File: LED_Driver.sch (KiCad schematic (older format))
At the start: 0 parts

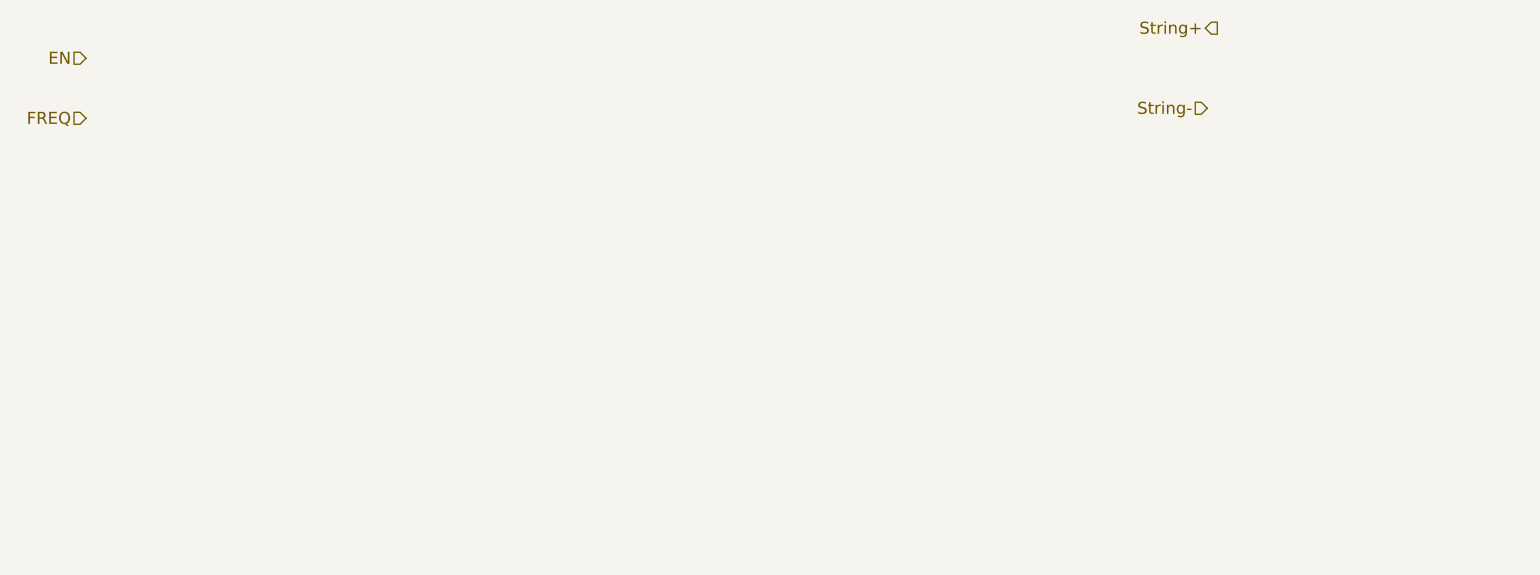
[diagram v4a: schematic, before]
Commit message: Added LED Driver Module Outline
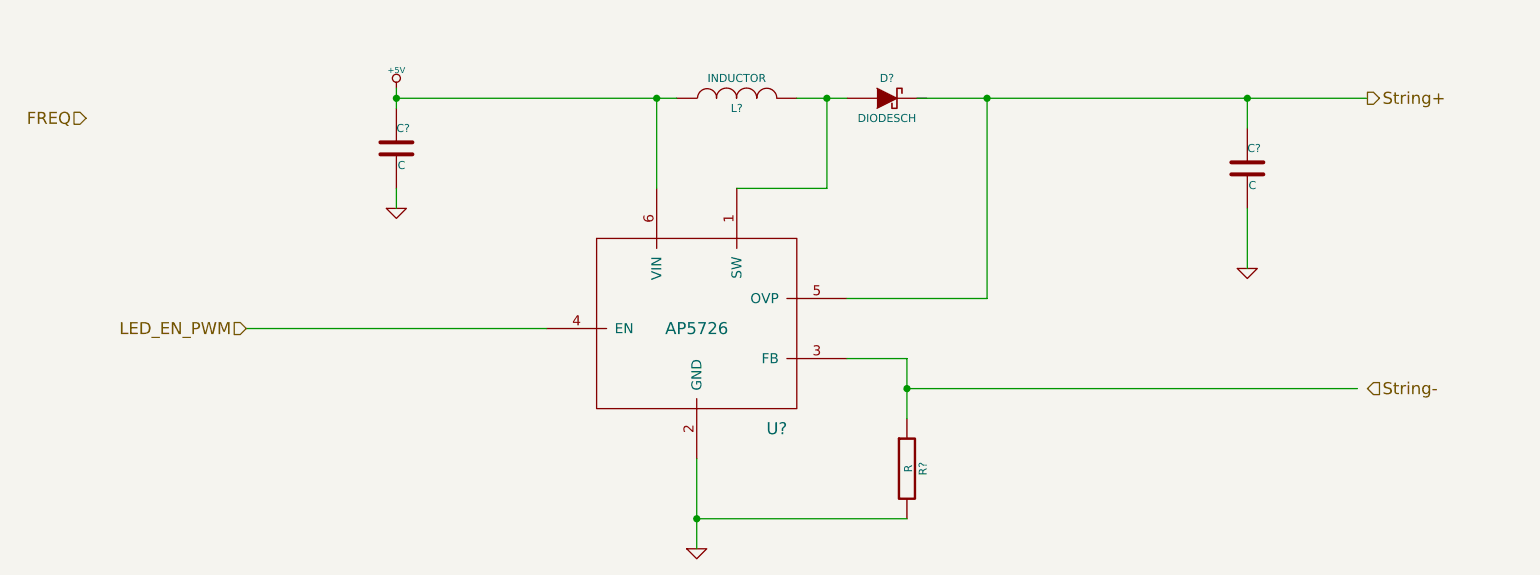
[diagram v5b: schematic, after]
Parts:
- added C? (x2): C, ~, symbol C
- added D?: DIODESCH, ~, symbol DIODESCH
- added L?: INDUCTOR, ~, symbol INDUCTOR
- added R?: R, ~, symbol R
- added U?: AP5726, symbol AP5726
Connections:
- net labels added: +5V, GND, LED_EN_PWM
- net labels removed: EN
- wire segments 0 -> 18
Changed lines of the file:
@@
 $Descr A4 11693 8268
 encoding utf-8
-Sheet 7 9
+Sheet 6 9
 Title ""
 Date "4 feb 2014"
@@
 Comment4 ""
 $EndDescr
-Text HLabel 2500 2350 0    60   Input ~ 0
-EN
+Text HLabel 3300 3700 0    60   Input ~ 0
+LED_EN_PWM
 Text HLabel 2500 2650 0    60   Input ~ 0
 FREQ
-Text HLabel 8150 2200 0    60   Output ~ 0
+Text HLabel 8900 2550 2    60   Output ~ 0
 String+
-Text HLabel 8100 2600 0    60   Input ~ 0
+Text HLabel 8900 4000 2    60   Input ~ 0
 String-
+$Comp
+L AP5726 U?
+U 1 1 52F0C98F
+P 5550 3700
+F 0 "U?" H 5950 3200 60  0000 C CNN
+F 1 "AP5726" H 5550 3700 60  0000 C CNN
+F 2 "" H 5550 3700 60  0000 C CNN
+F 3 "" H 5550 3700 60  0000 C CNN
+	1    5550 3700
+	1    0    0    -1
+$EndComp
+Wire Wire Line
+	3300 3700 4800 3700
+$Comp
+L +5V #PWR?
+U 1 1 52F0C9A4
+P 4050 2500
+F 0 "#PWR?" H 4050 2590 20  0001 C CNN
+F 1 "+5V" H 4050 2590 30  0000 C CNN
+F 2 "" H 4050 2500 60  0000 C CNN
+F 3 "" H 4050 2500 60  0000 C CNN
+	1    4050 2500
+	1    0    0    -1
+$EndComp
+$Comp
+L GND #PWR?
+U 1 1 52F0C9B3
+P 4050 3100
+F 0 "#PWR?" H 4050 3100 30  0001 C CNN
+F 1 "GND" H 4050 3030 30  0001 C CNN
+F 2 "" H 4050 3100 60  0000 C CNN
+F 3 "" H 4050 3100 60  0000 C CNN
+	1    4050 3100
+	1    0    0    -1
+$EndComp
+$Comp
+L GND #PWR?
+U 1 1 52F0C9C0
+P 5550 4800
+F 0 "#PWR?" H 5550 4800 30  0001 C CNN
+F 1 "GND" H 5550 4730 30  0001 C CNN
+F 2 "" H 5550 4800 60  0000 C CNN
+F 3 "" H 5550 4800 60  0000 C CNN
+	1    5550 4800
+	1    0    0    -1
+$EndComp
+$Comp
+L C C?
+U 1 1 52F0C9C8
+P 4050 2800
+F 0 "C?" H 4050 2900 40  0000 L CNN
+F 1 "C" H 4056 2715 40  0000 L CNN
+F 2 "~" H 4088 2650 30  0000 C CNN
+F 3 "~" H 4050 2800 60  0000 C CNN
+	1    4050 2800
+	1    0    0    -1
+$EndComp
+Wire Wire Line
+	4050 2500 4050 2600
+Wire Wire Line
+	4050 3000 4050 3100
+Wire Wire Line
+	4050 2550 5450 2550
+Wire Wire Line
+	5350 2550 5350 3000
+Connection ~ 4050 2550
+$Comp
+L INDUCTOR L?
+U 1 1 52F0C9F4
+P 5750 2550
+F 0 "L?" V 5700 2550 40  0000 C CNN
+F 1 "INDUCTOR" V 5850 2550 40  0000 C CNN
+F 2 "~" H 5750 2550 60  0000 C CNN
+F 3 "~" H 5750 2550 60  0000 C CNN
+	1    5750 2550
+	0    -1   -1   0
+$EndComp
+Connection ~ 5350 2550
+Wire Wire Line
+	5750 3000 6200 3000
+Wire Wire Line
+	6200 3000 6200 2550
+Wire Wire Line
+	6050 2550 6300 2550
+$Comp
+L DIODESCH D?
+U 1 1 52F0CA1B
+P 6500 2550
+F 0 "D?" H 6500 2650 40  0000 C CNN
+F 1 "DIODESCH" H 6500 2450 40  0000 C CNN
+F 2 "~" H 6500 2550 60  0000 C CNN
+F 3 "~" H 6500 2550 60  0000 C CNN
+	1    6500 2550
+	1    0    0    -1
+$EndComp
+Connection ~ 6200 2550
+Wire Wire Line
+	6650 2550 8900 2550
+$Comp
+L C C?
+U 1 1 52F0CA49
+P 8300 2900
+F 0 "C?" H 8300 3000 40  0000 L CNN
+F 1 "C" H 8306 2815 40  0000 L CNN
+F 2 "~" H 8338 2750 30  0000 C CNN
+F 3 "~" H 8300 2900 60  0000 C CNN
+	1    8300 2900
+	1    0    0    -1
+$EndComp
+Wire Wire Line
+	8300 2700 8300 2550
+Connection ~ 8300 2550
+Wire Wire Line
+	8300 3100 8300 3400
+$Comp
+L GND #PWR?
+U 1 1 52F0CA75
+P 8300 3400
+F 0 "#PWR?" H 8300 3400 30  0001 C CNN
+F 1 "GND" H 8300 3330 30  0001 C CNN
+F 2 "" H 8300 3400 60  0000 C CNN
+F 3 "" H 8300 3400 60  0000 C CNN
+	1    8300 3400
+	1    0    0    -1
+$EndComp
+Wire Wire Line
+	5550 4350 5550 4800
+$Comp
+L R R?
+U 1 1 52F0CAAA
+P 6600 4400
+F 0 "R?" V 6680 4400 40  0000 C CNN
+F 1 "R" V 6607 4401 40  0000 C CNN
+F 2 "~" V 6530 4400 30  0000 C CNN
+F 3 "~" H 6600 4400 30  0000 C CNN
+	1    6600 4400
+	1    0    0    -1
+$EndComp
+Wire Wire Line
+	6300 3850 6600 3850
+Wire Wire Line
+	6600 3850 6600 4150
+Wire Wire Line
+	6600 4650 5550 4650
+Connection ~ 5550 4650
+Wire Wire Line
+	8850 4000 6600 4000
+Connection ~ 6600 4000
+Wire Wire Line
+	7000 3550 7000 2550
+Connection ~ 7000 2550
+Wire Wire Line
+	7000 3550 6300 3550
 $EndSCHEMATC

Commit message: Hooked up top level schematic
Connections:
- net labels added: LED_STRING+, LED_STRING-
- net labels removed: String+, String-
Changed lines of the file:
@@
 FREQ
 Text HLabel 8900 2550 2    60   Output ~ 0
-String+
-Text HLabel 8900 4000 2    60   Input ~ 0
-String-
+LED_STRING+
+Text HLabel 8900 4000 2    60   Output ~ 0
+LED_STRING-
 $Comp
 L AP5726 U?
@@
 Connection ~ 5550 4650
 Wire Wire Line
-	8850 4000 6600 4000
+	6600 4000 8900 4000
 Connection ~ 6600 4000
 Wire Wire Line

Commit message: Fan Current module refactoring
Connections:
- net labels removed: FREQ
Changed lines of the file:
@@
 $Descr A4 11693 8268
 encoding utf-8
-Sheet 6 9
+Sheet 5 9
 Title ""
 Date "4 feb 2014"
@@
 Text HLabel 3300 3700 0    60   Input ~ 0
 LED_EN_PWM
-Text HLabel 2500 2650 0    60   Input ~ 0
-FREQ
 Text HLabel 8900 2550 2    60   Output ~ 0
 LED_STRING+

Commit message: Begin Associating relay Module
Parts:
- gave numbers to parts that had none: 6
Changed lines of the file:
@@
 LIBS:BenchBudEE
 LIBS:BenchBudEE-cache
-EELAYER 27 0
+EELAYER 24 0
 EELAYER END
 $Descr A4 11693 8268
@@
 LED_STRING-
 $Comp
-L AP5726 U?
+L AP5726 U5
 U 1 1 52F0C98F
 P 5550 3700
-F 0 "U?" H 5950 3200 60  0000 C CNN
+F 0 "U5" H 5950 3200 60  0000 C CNN
 F 1 "AP5726" H 5550 3700 60  0000 C CNN
 F 2 "" H 5550 3700 60  0000 C CNN
@@
 	3300 3700 4800 3700
 $Comp
-L +5V #PWR?
+L +5V #PWR26
 U 1 1 52F0C9A4
 P 4050 2500
-F 0 "#PWR?" H 4050 2590 20  0001 C CNN
+F 0 "#PWR26" H 4050 2590 20  0001 C CNN
 F 1 "+5V" H 4050 2590 30  0000 C CNN
 F 2 "" H 4050 2500 60  0000 C CNN
@@
 $EndComp
 $Comp
-L GND #PWR?
+L GND #PWR27
 U 1 1 52F0C9B3
 P 4050 3100
-F 0 "#PWR?" H 4050 3100 30  0001 C CNN
+F 0 "#PWR27" H 4050 3100 30  0001 C CNN
 F 1 "GND" H 4050 3030 30  0001 C CNN
 F 2 "" H 4050 3100 60  0000 C CNN
@@
 $EndComp
 $Comp
-L GND #PWR?
+L GND #PWR28
 U 1 1 52F0C9C0
 P 5550 4800
-F 0 "#PWR?" H 5550 4800 30  0001 C CNN
+F 0 "#PWR28" H 5550 4800 30  0001 C CNN
 F 1 "GND" H 5550 4730 30  0001 C CNN
 F 2 "" H 5550 4800 60  0000 C CNN
@@
 $EndComp
 $Comp
-L C C?
+L C C3
 U 1 1 52F0C9C8
 P 4050 2800
-F 0 "C?" H 4050 2900 40  0000 L CNN
+F 0 "C3" H 4050 2900 40  0000 L CNN
 F 1 "C" H 4056 2715 40  0000 L CNN
 F 2 "~" H 4088 2650 30  0000 C CNN
@@
 Connection ~ 4050 2550
 $Comp
-L INDUCTOR L?
+L INDUCTOR L3
 U 1 1 52F0C9F4
 P 5750 2550
-F 0 "L?" V 5700 2550 40  0000 C CNN
+F 0 "L3" V 5700 2550 40  0000 C CNN
 F 1 "INDUCTOR" V 5850 2550 40  0000 C CNN
 F 2 "~" H 5750 2550 60  0000 C CNN
@@
 	6050 2550 6300 2550
 $Comp
-L DIODESCH D?
+L DIODESCH D4
 U 1 1 52F0CA1B
 P 6500 2550
-F 0 "D?" H 6500 2650 40  0000 C CNN
+F 0 "D4" H 6500 2650 40  0000 C CNN
 F 1 "DIODESCH" H 6500 2450 40  0000 C CNN
 F 2 "~" H 6500 2550 60  0000 C CNN
@@
 	6650 2550 8900 2550
 $Comp
-L C C?
+L C C4
 U 1 1 52F0CA49
 P 8300 2900
-F 0 "C?" H 8300 3000 40  0000 L CNN
+F 0 "C4" H 8300 3000 40  0000 L CNN
 F 1 "C" H 8306 2815 40  0000 L CNN
 F 2 "~" H 8338 2750 30  0000 C CNN
@@
 	8300 3100 8300 3400
 $Comp
-L GND #PWR?
+L GND #PWR29
 U 1 1 52F0CA75
 P 8300 3400
-F 0 "#PWR?" H 8300 3400 30  0001 C CNN
+F 0 "#PWR29" H 8300 3400 30  0001 C CNN
 F 1 "GND" H 8300 3330 30  0001 C CNN
 F 2 "" H 8300 3400 60  0000 C CNN
@@
 	5550 4350 5550 4800
 $Comp
-L R R?
+L R R15
 U 1 1 52F0CAAA
 P 6600 4400
-F 0 "R?" V 6680 4400 40  0000 C CNN
+F 0 "R15" V 6680 4400 40  0000 C CNN
 F 1 "R" V 6607 4401 40  0000 C CNN
 F 2 "~" V 6530 4400 30  0000 C CNN
